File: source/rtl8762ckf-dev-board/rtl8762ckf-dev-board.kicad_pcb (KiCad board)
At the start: 2 copper layers, 97.8 x 17.8 mm, 140 parts, among them J1 boot, J2 Conn_02x05_Odd_Even, J3 Conn_02x05_Odd_Even, J4 Conn_01x13, J5 Conn_01x18, J6 u.FL, J7 USB_C_Receptacle_USB2.0, Q2 AO3401A, Q3 Dual_PNP, SW1 SW_Push, U1 ME6211C33M5G-N, U2 RTL8762CKF, U3 USBLC6-2SC6, U5 W25Q16JV, U6 RP2040, U7 W25Q128JVS, Y1 40MHz, Y2 12M

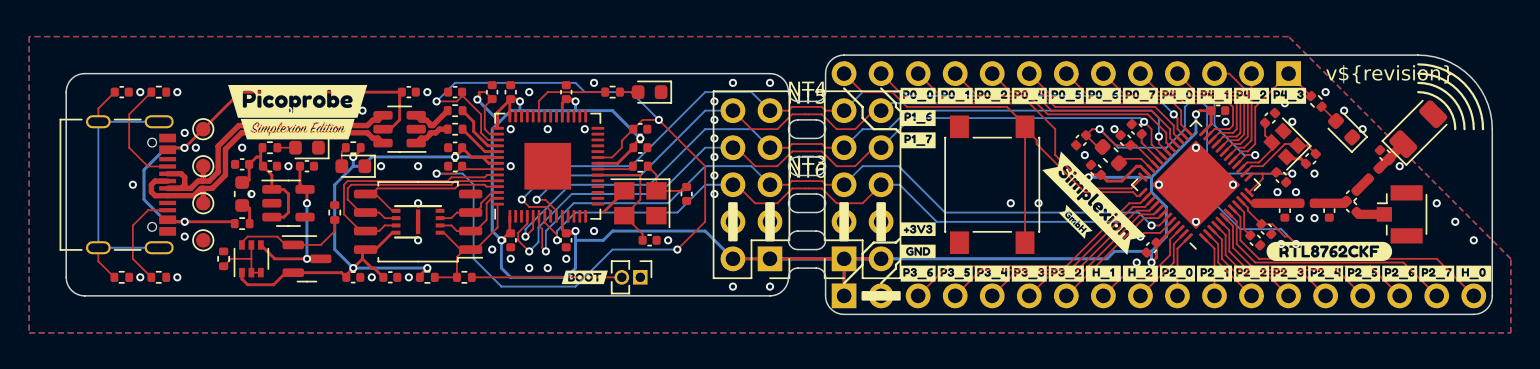
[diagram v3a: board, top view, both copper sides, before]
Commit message: embiggen silk screen text; #3
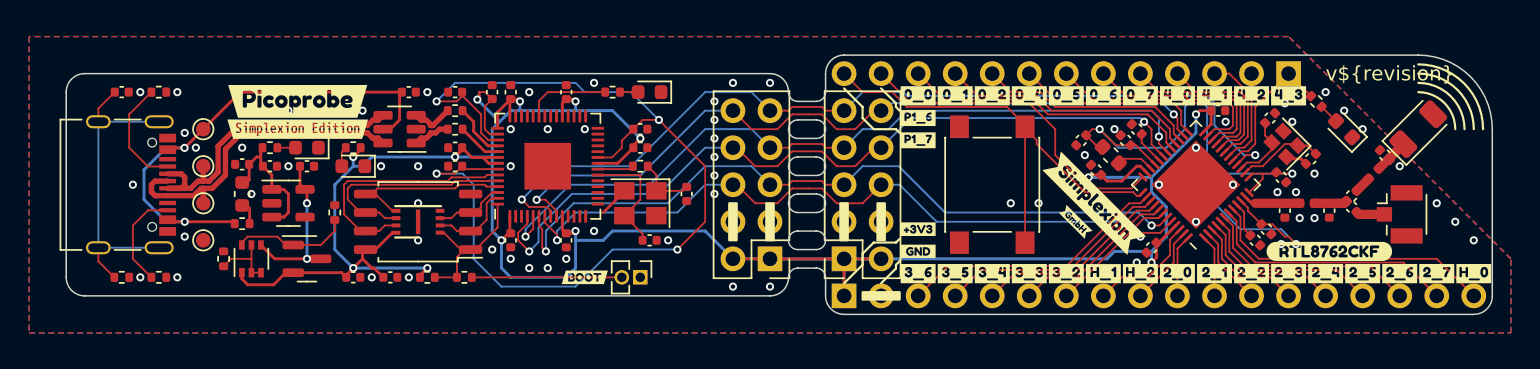
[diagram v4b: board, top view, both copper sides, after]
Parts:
- removed kibuzzard-641CA399: G***, kibuzzard-641CA399
- removed kibuzzard-641CA39E: G***, kibuzzard-641CA39E
- removed kibuzzard-641CA3A8: G***, kibuzzard-641CA3A8
- removed kibuzzard-641CA3B1: G***, kibuzzard-641CA3B1
- removed kibuzzard-641CA3B7: G***, kibuzzard-641CA3B7
- removed kibuzzard-641CA3BC: G***, kibuzzard-641CA3BC
- removed kibuzzard-641CA3C1: G***, kibuzzard-641CA3C1
- removed kibuzzard-641CA3C6: G***, kibuzzard-641CA3C6
- removed kibuzzard-641CA3CB: G***, kibuzzard-641CA3CB
- removed kibuzzard-641CA3D0: G***, kibuzzard-641CA3D0
- removed kibuzzard-641CA3D4: G***, kibuzzard-641CA3D4
- removed kibuzzard-641CA3D9: G***, kibuzzard-641CA3D9
- removed kibuzzard-641CA40F: G***, kibuzzard-641CA40F
- removed kibuzzard-641CA415: G***, kibuzzard-641CA415
- removed kibuzzard-641CA41A: G***, kibuzzard-641CA41A
- removed kibuzzard-641CA41F: G***, kibuzzard-641CA41F
- removed kibuzzard-641CA424: G***, kibuzzard-641CA424
- removed kibuzzard-641CA429: G***, kibuzzard-641CA429
- removed kibuzzard-641CA42E: G***, kibuzzard-641CA42E
- removed kibuzzard-641CA433: G***, kibuzzard-641CA433
- removed kibuzzard-641CA439: G***, kibuzzard-641CA439
- removed kibuzzard-641CCF1B: G***, kibuzzard-641CCF1B
- removed kibuzzard-641CCF27: G***, kibuzzard-641CCF27
- removed kibuzzard-641CCF2F: G***, kibuzzard-641CCF2F
- removed kibuzzard-641CCF34: G***, kibuzzard-641CCF34
- removed kibuzzard-641CCFE3: G***, kibuzzard-641CCFE3
- removed kibuzzard-641CCFE7: G***, kibuzzard-641CCFE7
- removed kibuzzard-642D5F02: G***, kibuzzard-642D5F02
- added kibuzzard-643FF35A: G***, kibuzzard-643FF35A, F.Cu at (185.4, 120.9)
- added kibuzzard-643FF367: G***, kibuzzard-643FF367, F.Cu at (188.0, 120.9)
- added kibuzzard-643FF370: G***, kibuzzard-643FF370, F.Cu at (190.5, 120.9)
- added kibuzzard-643FF37A: G***, kibuzzard-643FF37A, F.Cu at (193.0, 120.9)
- added kibuzzard-643FF387: G***, kibuzzard-643FF387, F.Cu at (195.6, 120.9)
- added kibuzzard-643FF393: G***, kibuzzard-643FF393, F.Cu at (198.1, 120.9)
- added kibuzzard-643FF39C: G***, kibuzzard-643FF39C, F.Cu at (200.7, 120.9)
- added kibuzzard-643FF3A2: G***, kibuzzard-643FF3A2, F.Cu at (203.2, 120.9)
- added kibuzzard-643FF3AF: G***, kibuzzard-643FF3AF, F.Cu at (205.7, 120.9)
- added kibuzzard-643FF3B6: G***, kibuzzard-643FF3B6, F.Cu at (208.3, 120.9)
- added kibuzzard-643FF3C1: G***, kibuzzard-643FF3C1, F.Cu at (210.8, 120.9)
- added kibuzzard-643FF3D9: G***, kibuzzard-643FF3D9, F.Cu at (185.4, 133.1)
- added kibuzzard-643FF3DF: G***, kibuzzard-643FF3DF, F.Cu at (188.0, 133.1)
- added kibuzzard-643FF3E8: G***, kibuzzard-643FF3E8, F.Cu at (190.5, 133.1)
- added kibuzzard-643FF3F7: G***, kibuzzard-643FF3F7, F.Cu at (193.0, 133.1)
- added kibuzzard-643FF3FE: G***, kibuzzard-643FF3FE, F.Cu at (195.6, 133.1)
- added kibuzzard-643FF404: G***, kibuzzard-643FF404, F.Cu at (198.1, 133.1)
- added kibuzzard-643FF40B: G***, kibuzzard-643FF40B, F.Cu at (200.7, 133.1)
- added kibuzzard-643FF41C: G***, kibuzzard-643FF41C, F.Cu at (203.2, 133.1)
- added kibuzzard-643FF422: G***, kibuzzard-643FF422, F.Cu at (205.7, 133.1)
- added kibuzzard-643FF427: G***, kibuzzard-643FF427, F.Cu at (208.3, 133.1)
- added kibuzzard-643FF42D: G***, kibuzzard-643FF42D, F.Cu at (210.8, 133.1)
- added kibuzzard-643FF432: G***, kibuzzard-643FF432, F.Cu at (213.4, 133.1)
- added kibuzzard-643FF439: G***, kibuzzard-643FF439, F.Cu at (215.9, 133.1)
- added kibuzzard-643FF440: G***, kibuzzard-643FF440, F.Cu at (218.4, 133.1)
- added kibuzzard-643FF446: G***, kibuzzard-643FF446, F.Cu at (221.0, 133.1)
- added kibuzzard-643FF44A: G***, kibuzzard-643FF44A, F.Cu at (223.5, 133.1)
- added kibuzzard-643FF486: G***, kibuzzard-643FF486, F.Cu at (142.9, 123.2)

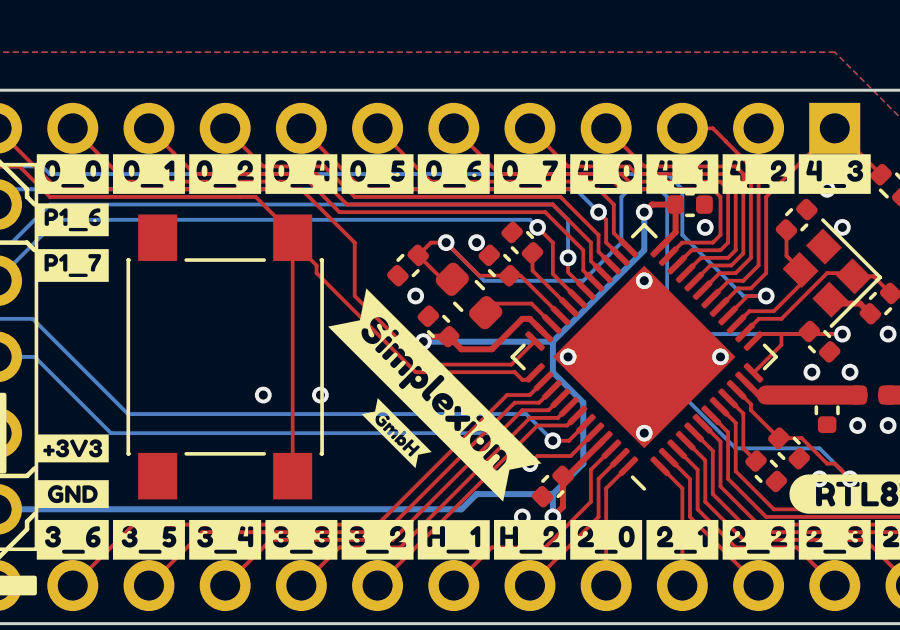
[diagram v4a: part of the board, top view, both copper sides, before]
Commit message: change part number of RTL8762C power inductor; closes #2
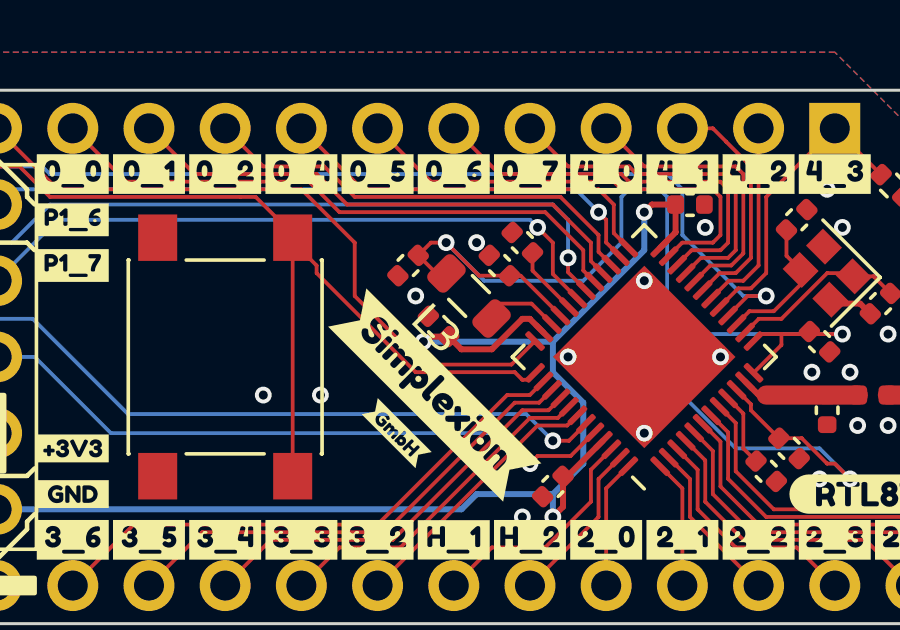
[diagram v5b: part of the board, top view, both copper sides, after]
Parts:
- L3: footprint Inductor_SMD:L_0603_1608Metric -> Inductor_SMD:L_0805_2012Metric
